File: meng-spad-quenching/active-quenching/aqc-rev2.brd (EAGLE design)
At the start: 120 x 74.9 mm, 294 parts, among them IC1 ADCMP582, IC10 74AHC1G04DBV, IC11 74AHC1G04DBV, IC12 TLV272DGK, IC13 TLV271DBV, IC14 74AHC1G04DBV, IC15 ALD1106, IC16 ALD1107, IC17 74AHC1G04DBV, IC18 LT1534-1, IC19 LT1534-1, IC2 TLV271DBV, IC20 STM32F411RE, IC22 TPS7A3001, IC24 TPS7A4901, IC25 TPS7A4901, IC27 USBLC6-2SC6Y, IC28 MAX572X, IC3 NC7SV74K8X, IC4 TLV272DGK, IC5 NC7WZ16P6X, IC6 LTC1711, IC7 DS1100LU-20+, IC8 LM1117, M1 BSS806N, M2 BSS806N, M3 BSS806N, Q1 IRLML6402TRPBF, Q2 MMBTH81, Q3 MMBTH81, Q5 MMBTH81, Q7 MMBTH81, Q8 MMBTH81, SW1 MCU_RST, T1 MMBTH10, T2 MMBTH10, T5 MMBTH10, T6 MMBTH10, T7 MMBTH10, T8 MMBTH10, T9 MMBTH10, U1 SN65EPT21DGK, U2 SN65EPT22DGK, X1 CONN_SPAD, X2 CONN_PHOTON_COUNTER, X3 KEYSTONE-7774, X4 KEYSTONE-7774, X5 CONN_SMU, X6 CONN_FORCE_QUENCH, X7 CONN_PULLDN_SENSE, X8 PN61729-S

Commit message: misc cleanup
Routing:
- net GND: track 316.5 -> 326.0 mm, vias 354 -> 356
- net FORCE_QUENCH: track 70.4 -> 71.9 mm, vias 1 -> 2
- net PHOTON_COUNT_OUT: track 48.4 -> 49.5 mm, vias 1 -> 2
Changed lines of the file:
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@@
 </element>
 <element name="R28" library="rcl" package="R0603" value="49R9" x="67.6275" y="42.545" smashed="yes" rot="R180">
-<attribute name="NAME" x="69.5325" y="42.2275" size="0.8128" layer="25" font="vector" ratio="16"/>
+<attribute name="NAME" x="67.31" y="43.4975" size="0.8128" layer="25" font="vector" ratio="16"/>
 </element>
 <element name="TP4" library="testpad" package="TP15R" value="TPTP15R" x="98.1075" y="69.85" smashed="yes">
@@
 </element>
 <element name="R22" library="rcl" package="R0603" value="49R9" x="67.6275" y="40.3225" smashed="yes">
-<attribute name="NAME" x="69.5325" y="40.005" size="0.8128" layer="25" font="vector" ratio="16"/>
+<attribute name="NAME" x="69.5325" y="39.6875" size="0.8128" layer="25" font="vector" ratio="16"/>
 </element>
 <element name="X6" library="meng" package="J502-ND-142-0711-871/876" value="CONN_FORCE_QUENCH" x="118.4275" y="15.875" smashed="yes" rot="R180">
@@
 <wire x1="85.305" y1="51.1175" x2="84.9875" y2="51.435" width="0.4064" layer="1"/>
 <wire x1="60.325" y1="37.7975" x2="61.595" y2="37.7975" width="0.4064" layer="1"/>
-<wire x1="86.36" y1="62.5475" x2="84.9875" y2="62.5475" width="0" layer="19" extent="1-1"/>
+<wire x1="61.595" y1="37.7975" x2="61.8975" y2="37.7975" width="0.4064" layer="1"/>
+<wire x1="62.5475" y1="37.1475" x2="64.4525" y2="37.1475" width="0.4064" layer="1"/>
+<wire x1="64.4525" y1="37.1475" x2="65.405" y2="38.1" width="0.4064" layer="1"/>
+<wire x1="65.405" y1="38.1" x2="66.0575" y2="38.1" width="0.4064" layer="1"/>
+<wire x1="66.0575" y1="38.1" x2="66.06" y2="38.0975" width="0.4064" layer="1"/>
+<wire x1="61.8975" y1="37.7975" x2="62.5475" y2="37.1475" width="0.4064" layer="1"/>
+<wire x1="86.36" y1="62.5475" x2="84.9875" y2="62.5475" width="0.4064" layer="1"/>
+<wire x1="91.7575" y1="11.43" x2="90.805" y2="11.43" width="0.6096" layer="1"/>
+<via x="91.7575" y="11.43" extent="1-16" drill="0.3" alwaysstop="yes"/>
+<via x="90.805" y="11.43" extent="1-16" drill="0.3" alwaysstop="yes"/>
+<wire x1="92.71" y1="9.7825" x2="92.71" y2="10.4775" width="0.6096" layer="1"/>
+<wire x1="92.71" y1="10.4775" x2="91.7575" y2="11.43" width="0.6096" layer="1"/>
+<wire x1="66.06" y1="38.0975" x2="66.7775" y2="40.3225" width="0" layer="19" extent="1-1"/>
+<wire x1="62.65" y1="42.545" x2="66.7775" y2="40.3225" width="0" layer="19" extent="1-1"/>
 <wire x1="46.6725" y1="33.235" x2="46.6725" y2="33.02" width="0" layer="19" extent="1-1"/>
-<wire x1="92.71" y1="9.7825" x2="92.3925" y2="13.6525" width="0" layer="19" extent="1-1"/>
-<wire x1="66.7775" y1="40.3225" x2="62.65" y2="42.545" width="0" layer="19" extent="1-1"/>
-<wire x1="66.06" y1="38.0975" x2="66.7775" y2="40.3225" width="0" layer="19" extent="1-1"/>
-<wire x1="61.595" y1="37.7975" x2="66.06" y2="38.0975" width="0" layer="19" extent="1-1"/>
 <wire x1="44.3025" y1="46.035" x2="41.91" y2="41.06" width="0" layer="19" extent="1-1"/>
 </signal>
@@
 <via x="113.9825" y="37.465" extent="1-16" drill="0.35" alwaysstop="yes"/>
 <wire x1="113.9825" y1="37.465" x2="115.8621" y2="37.465" width="0.254" layer="1"/>
-<wire x1="108.9025" y1="42.545" x2="69.5325" y2="42.545" width="0.254" layer="16"/>
+<wire x1="108.9025" y1="42.545" x2="71.12" y2="42.545" width="0.254" layer="16"/>
 <wire x1="113.9825" y1="37.465" x2="108.9025" y2="42.545" width="0.254" layer="16"/>
-<wire x1="68.4775" y1="42.545" x2="69.5325" y2="42.545" width="0" layer="19" extent="1-16"/>
+<via x="71.12" y="42.545" extent="1-16" drill="0.35" alwaysstop="yes"/>
+<wire x1="68.4775" y1="42.545" x2="71.12" y2="42.545" width="0.254" layer="1"/>
 </signal>
 <signal name="COMP_Q_P" class="1">
@@
 <wire x1="108.9025" y1="17.145" x2="108.9025" y2="40.3225" width="0.254" layer="16"/>
 <wire x1="108.9025" y1="40.3225" x2="107.95" y2="41.275" width="0.254" layer="16"/>
-<wire x1="107.95" y1="41.275" x2="69.5325" y2="41.275" width="0.254" layer="16"/>
-<wire x1="68.4775" y1="40.3225" x2="69.5325" y2="41.275" width="0" layer="19" extent="1-16"/>
+<wire x1="107.95" y1="41.275" x2="71.12" y2="41.275" width="0.254" layer="16"/>
+<via x="71.12" y="41.275" extent="1-16" drill="0.35" alwaysstop="yes"/>
+<wire x1="71.12" y1="41.275" x2="69.43" y2="41.275" width="0.254" layer="1"/>
+<wire x1="69.43" y1="41.275" x2="68.4775" y2="40.3225" width="0.254" layer="1"/>
 <wire x1="66.06" y1="37.1475" x2="68.4775" y2="40.3225" width="0" layer="19" extent="1-1"/>
 </signal>

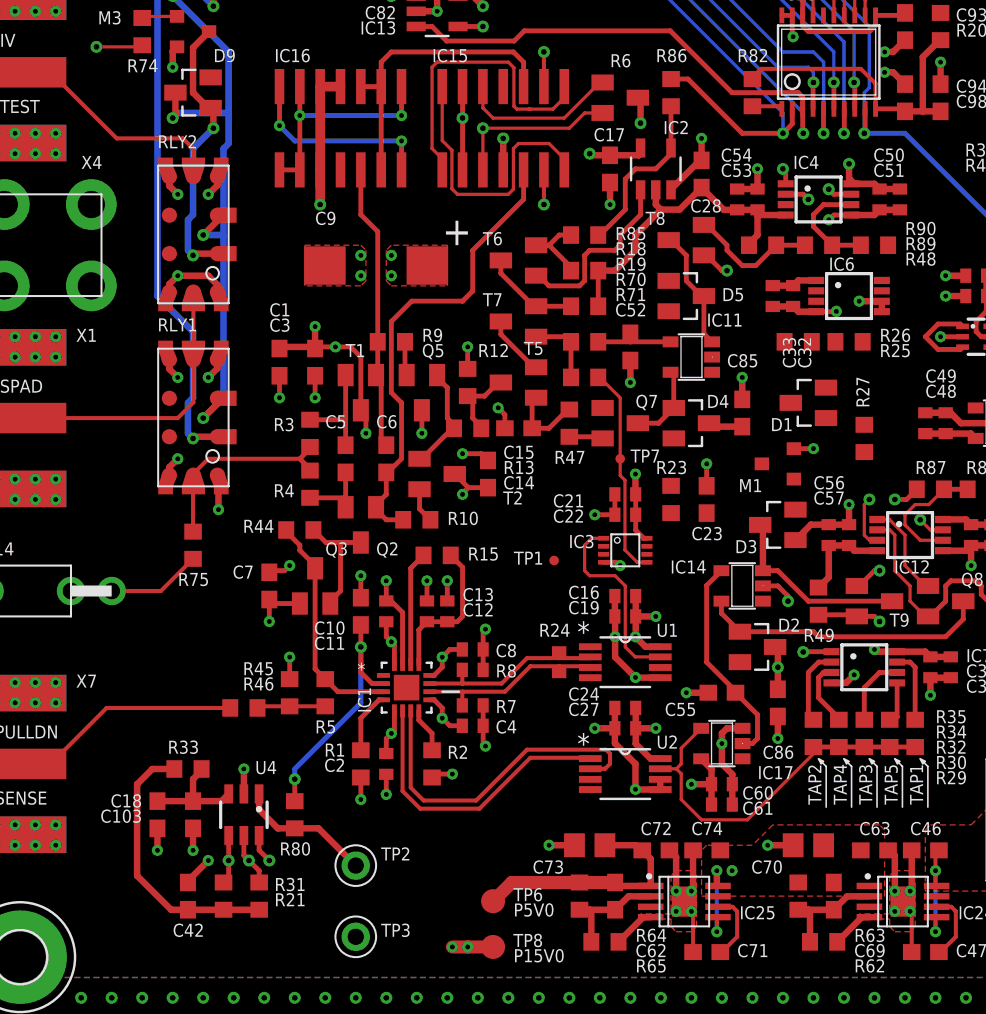
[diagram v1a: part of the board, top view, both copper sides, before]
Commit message: more routing, connected all 5V0 nets to analog 5V0
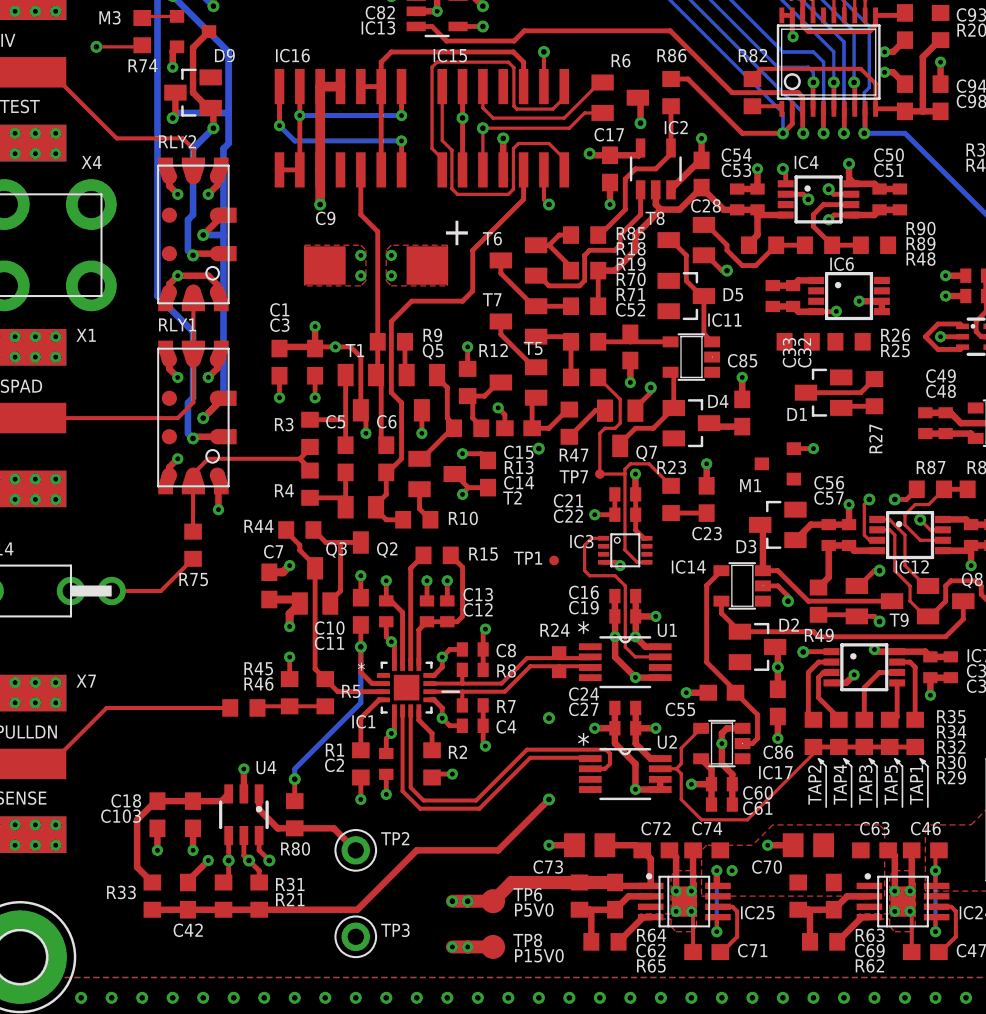
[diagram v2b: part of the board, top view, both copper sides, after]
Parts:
- moved R33 8.24 mm to (12.1, 7.62), turned to 90 degrees
- moved R27 2.93 mm to (57.1, 39.1), turned to 90 degrees
- moved TP7 1.59 mm to (40.0, 34.0)
- moved D1 1.14 mm to (54.0, 39.1)
- moved TP2 0.95 mm to (24.8, 10.5)
- moved Q7 0.32 mm to (41.3, 36.8), turned to 180 degrees
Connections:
- removed net PP_P5V0: C11.1, C15.1, C17.1, C2.1, C50.1, C51.1, C58.1, C59.1, C7.1, C82.1, IC1.16, IC1.5, IC12.8, IC13.5, IC15.6, IC15.9, IC2.5, IC4.8, Q3.B, R20.1, R47.2, R50.2, T5.B
- net PP_P5V0_ANALOG: now also C11.1, C15.1, C17.1, C2.1, C50.1, C51.1, C58.1, C59.1, C7.1, C82.1, IC1.16, IC1.5, IC12.8, IC13.5, IC15.6, IC15.9, IC2.5, IC4.8, Q3.B, R20.1, R47.2, R50.2, T5.B
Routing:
- net PP_P5V0_ANALOG: track 15.3 -> 155.6 mm, vias 0 -> 11
- net PP_P5V0: track 81.5 -> 0.00 mm, vias 8 -> 0
- net PP_P3V3: track 331.0 -> 346.8 mm, vias 13 -> 15
- net LOGIC_QUENCH: track 18.6 -> 24.8 mm
- net N$36: track 0.00 -> 4.63 mm
- net PP_P3V3_DAC2: track 6.86 -> 10.7 mm
- net ONE_SHOT_CAP: track 0.00 -> 2.22 mm
- net ONE_SHOT_CLR: track 0.00 -> 2.12 mm
- net N$38: track 1.00 -> 2.84 mm, vias 1 -> 2
- net N$7: track 4.95 -> 6.72 mm
- net N$1: track 3.67 -> 4.45 mm

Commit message: more routing
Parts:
- moved M1 1.62 mm to (49.5, 34.3), turned to 180 degrees
- moved TP8 1.27 mm to (33.3, 5.71)
- moved TP6 0.95 mm to (33.3, 8.26)
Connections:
- removed net PP_P15V0: C1.1, C14.1, C3.1, C9.+, IC16.11, IC16.12, IC16.3, R12.2, T1.C, T2.C
- net PP_P15V0_ANALOG: now also C1.1, C14.1, C3.1, C9.+, IC16.11, IC16.12, IC16.3, R12.2, T1.C, T2.C
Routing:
- net PP_P15V0_ANALOG: track 26.9 -> 87.4 mm, vias 5 -> 13
- net PP_P5V0_ANALOG: track 155.6 -> 192.6 mm
- net PP_P15V0: track 24.7 -> 0.00 mm, vias 8 -> 0
- net VREF_SLEW_DN: track 22.4 -> 35.7 mm
- net N$25: track 0.00 -> 6.50 mm
- net PP_P3V3: track 346.8 -> 350.6 mm
- net GND: track 325.9 -> 329.7 mm, vias 356 -> 357
- net ONE_SHOT_CAP: track 2.22 -> 5.81 mm
- net N$42: track 12.7 -> 12.1 mm
- added copper zone on layer 15, net PP_P15V0_ANALOG
- removed copper zone on layer 1, net PP_P15V0
- removed copper zone on layer 15, net PP_P15V0

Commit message: More routing
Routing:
- net !ONE_SHOT_CLR: track 0.00 -> 29.7 mm
- net !LOGIC_QUENCH: track 0.00 -> 11.7 mm
- net ONE_SHOT_CLR: track 2.12 -> 12.9 mm
- net ONE_SHOT_CAP: track 5.81 -> 15.6 mm
- net PP_P3V3: track 350.6 -> 357.8 mm, vias 15 -> 16
- net N$36: track 4.63 -> 9.41 mm

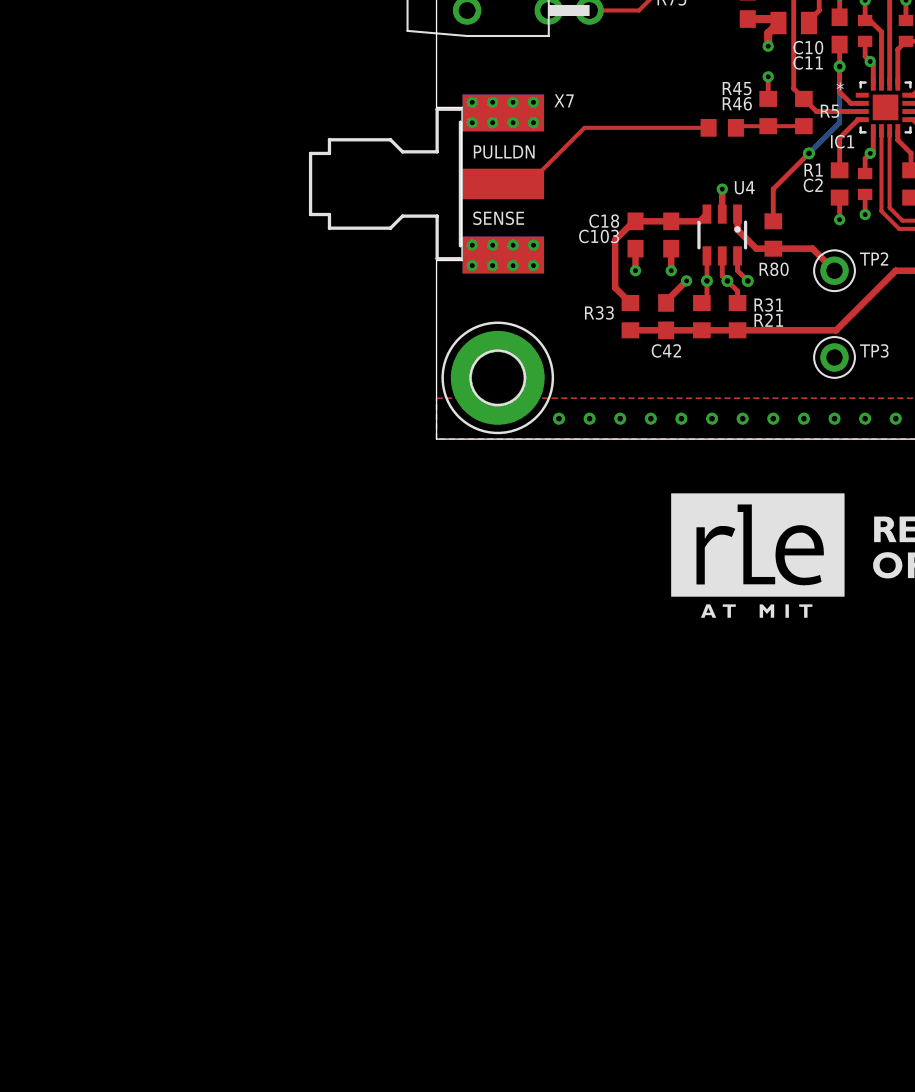
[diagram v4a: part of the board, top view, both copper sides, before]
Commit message: Added RC filter to discriminator as an option
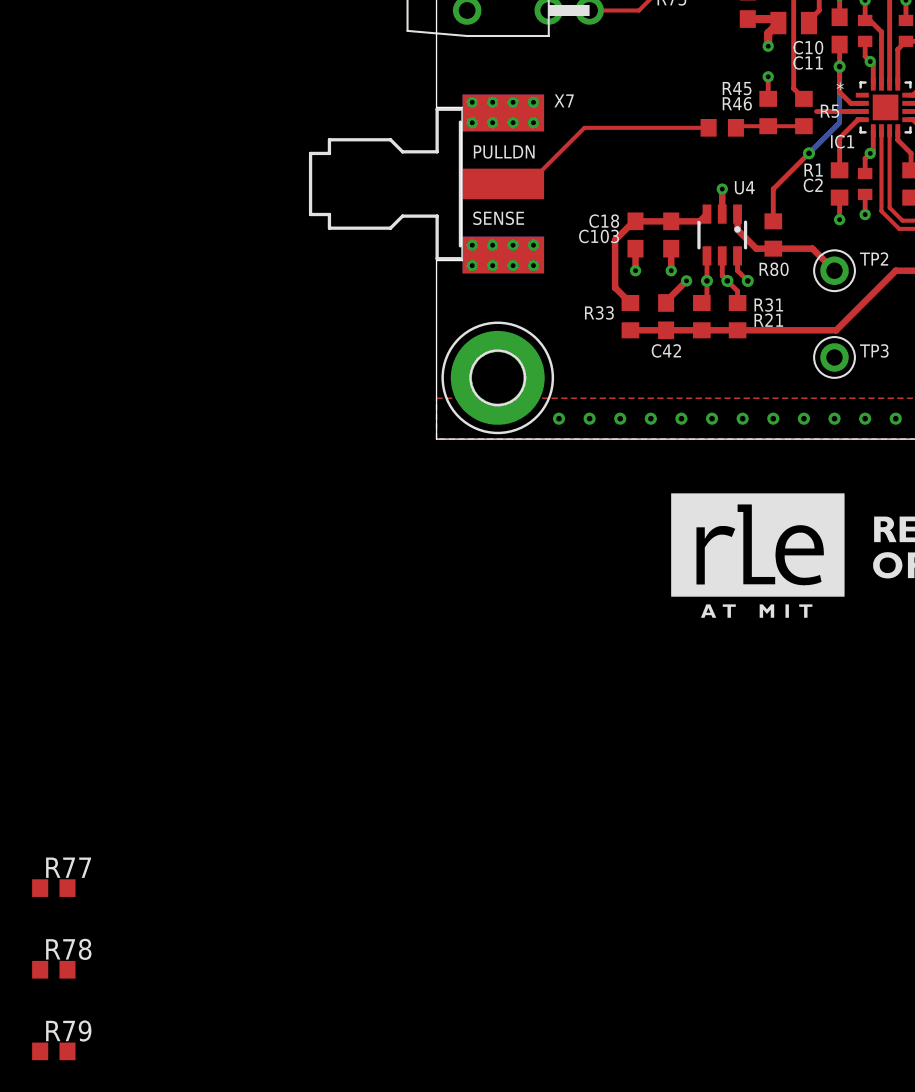
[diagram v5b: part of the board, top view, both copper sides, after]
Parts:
- added R77: 0R, rcl:R0603
- added R78, R79: DNP, rcl:R0603
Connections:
- new net N$27: Q3.C, R44.1, R5.2, R77.2
- net GND: now also R79.1
- net N$32: now also R78.1
- net SPAD_PULLDN_SENSE: now also R77.1, R78.2, R79.2; no longer Q3.C, R44.1, R5.2
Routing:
- net SPAD_PULLDN_SENSE: track 14.3 -> 2.85 mm
- net N$27: track 0.00 -> 10.3 mm
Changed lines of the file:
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@@
 <attribute name="VALUE" x="116.84" y="47.3075" size="1.27" layer="27" rot="R90"/>
 </element>
+<element name="R77" library="rcl" package="R0603" value="0R" x="-23.8125" y="-27.94"/>
+<element name="R78" library="rcl" package="R0603" value="DNP" x="-23.8125" y="-33.02"/>
+<element name="R79" library="rcl" package="R0603" value="DNP" x="-23.8125" y="-38.1"/>
 </elements>
 <signals>
@@
 <wire x1="66.06" y1="38.0975" x2="67.3075" y2="38.0975" width="0.4064" layer="1"/>
 <wire x1="67.3075" y1="38.0975" x2="67.31" y2="38.1" width="0.4064" layer="1"/>
+<contactref element="R79" pad="1"/>
 <wire x1="67.31" y1="38.1" x2="66.7775" y2="40.3225" width="0" layer="19" extent="1-1"/>
+<wire x1="-24.6625" y1="-38.1" x2="3.81" y2="3.81" width="0" layer="19" extent="1-1"/>
 </signal>
 <signal name="VBB">
@@
 </signal>
 <signal name="SPAD_PULLDN_SENSE">
-<contactref element="R5" pad="2"/>
 <contactref element="IC1" pad="3"/>
-<contactref element="Q3" pad="C"/>
-<contactref element="R44" pad="1"/>
-<wire x1="20.4225" y1="30.3775" x2="20.4225" y2="30.48" width="0.3048" layer="1"/>
-<wire x1="20.4225" y1="30.3775" x2="21.2725" y2="29.5275" width="0.3048" layer="1"/>
-<wire x1="21.2725" y1="29.5275" x2="21.2725" y2="29.21" width="0.3048" layer="1"/>
-<wire x1="22.225" y1="28.2575" x2="21.2725" y2="29.21" width="0.3048" layer="1"/>
-<wire x1="22.225" y1="28.2575" x2="22.225" y2="28.0875" width="0.3048" layer="1"/>
-<wire x1="22.86" y1="21.17" x2="22.225" y2="21.805" width="0.3048" layer="1"/>
-<wire x1="22.225" y1="28.0875" x2="22.225" y2="21.805" width="0.3048" layer="1"/>
-<wire x1="23.6465" y1="20.3835" x2="22.86" y2="21.17" width="0.3048" layer="1"/>
 <wire x1="26.4922" y1="20.3835" x2="23.6465" y2="20.3835" width="0.3048" layer="1"/>
+<contactref element="R77" pad="1"/>
+<contactref element="R78" pad="2"/>
+<contactref element="R79" pad="2"/>
+<wire x1="-22.9625" y1="-33.02" x2="-22.9625" y2="-38.1" width="0" layer="19" extent="1-1"/>
+<wire x1="-24.6625" y1="-27.94" x2="-22.9625" y2="-33.02" width="0" layer="19" extent="1-1"/>
+<wire x1="23.6465" y1="20.3835" x2="-24.6625" y2="-27.94" width="0" layer="19" extent="1-1"/>
 </signal>
 <signal name="CASC_MIDPT">
@@
 <wire x1="16.93" y1="19.3675" x2="9.2075" y2="19.3675" width="0.254" layer="1"/>
 <wire x1="9.2075" y1="19.3675" x2="5.715" y2="15.875" width="0.254" layer="1"/>
+<contactref element="R78" pad="1"/>
+<wire x1="4.1529" y1="15.875" x2="-24.6625" y2="-33.02" width="0" layer="19" extent="1-1"/>
 </signal>
 <signal name="N$42">
@@
 <wire x1="91.1225" y1="48.26" x2="109.855" y2="48.26" width="0.4064" layer="16"/>
 </signal>
+<signal name="N$27">
+<contactref element="R5" pad="2"/>
+<contactref element="Q3" pad="C"/>
+<contactref element="R44" pad="1"/>
+<contactref element="R77" pad="2"/>
+<wire x1="20.4225" y1="30.3775" x2="20.4225" y2="30.48" width="0.3048" layer="1"/>
+<wire x1="20.4225" y1="30.3775" x2="21.2725" y2="29.5275" width="0.3048" layer="1"/>
+<wire x1="21.2725" y1="29.5275" x2="21.2725" y2="29.21" width="0.3048" layer="1"/>
+<wire x1="22.225" y1="28.2575" x2="21.2725" y2="29.21" width="0.3048" layer="1"/>
+<wire x1="22.225" y1="28.2575" x2="22.225" y2="28.0875" width="0.3048" layer="1"/>
+<wire x1="22.86" y1="21.17" x2="22.225" y2="21.805" width="0.3048" layer="1"/>
+<wire x1="22.225" y1="28.0875" x2="22.225" y2="21.805" width="0.3048" layer="1"/>
+<wire x1="22.86" y1="21.17" x2="-22.9625" y2="-27.94" width="0" layer="19" extent="1-1"/>
+</signal>
 </signals>
